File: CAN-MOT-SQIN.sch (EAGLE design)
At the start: 24 parts, among them U1 TLV760, U2 MCP25625ML, U3 BTM7752G, U4 ATTINY816M, Y1 16MHz

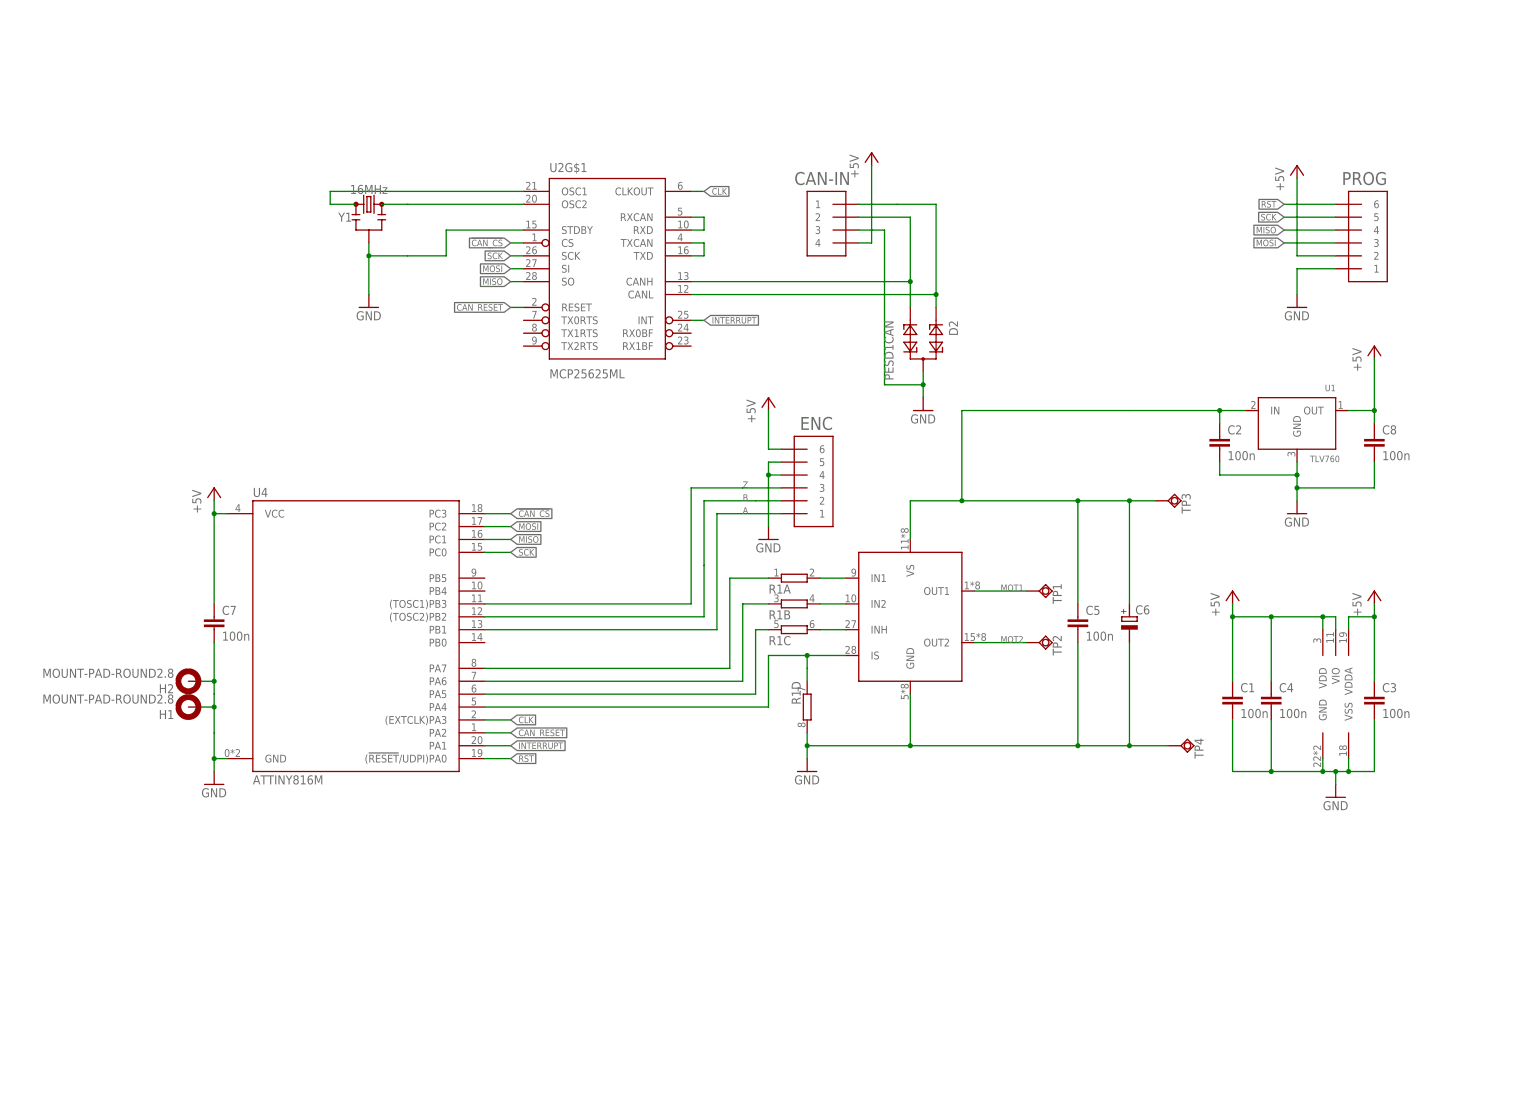
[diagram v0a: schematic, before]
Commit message: Now with better silkscreen
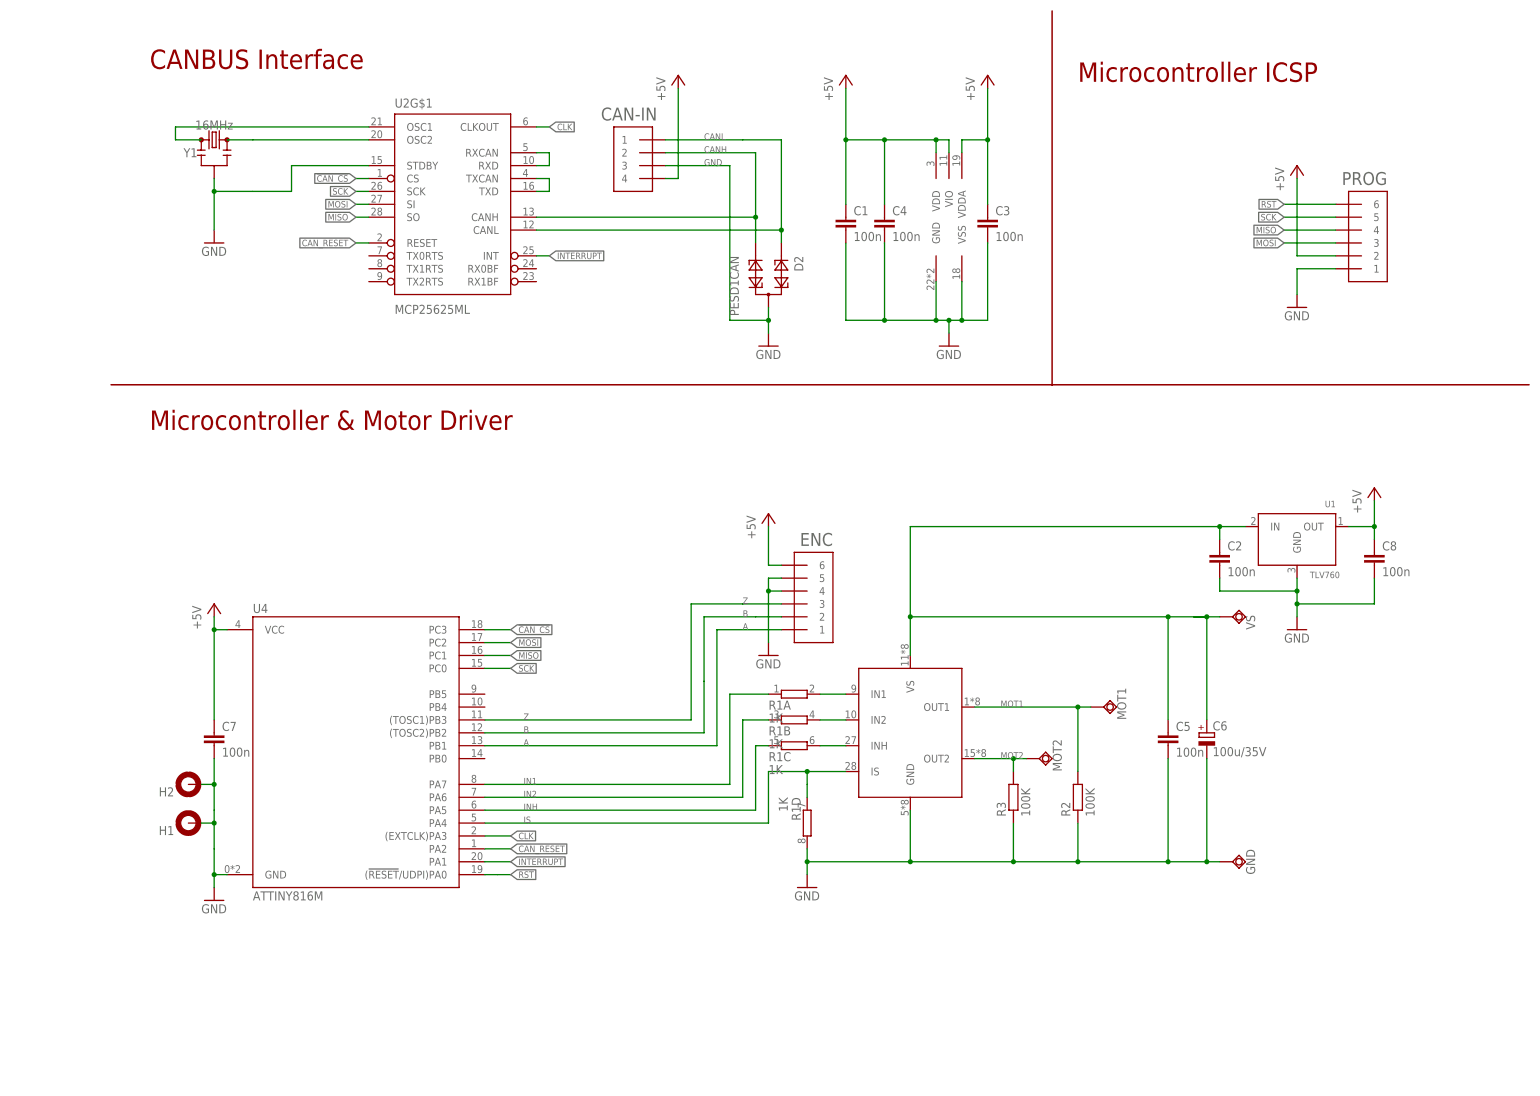
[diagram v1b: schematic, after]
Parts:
- removed TP1, TP2, TP3, TP4: TPSQTP20SQ, testpad:TPSQTP20SQ
- added GND, MOT1, MOT2, VS: TPSQTP20SQ, testpad:TPSQTP20SQ
- added R2, R3: 100K, resistor:R-EU_R0603
- C6: value (none) -> 100u/35V
- R1: value (none) -> 1K
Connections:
- net N$12 renamed IN2
- net N$13 renamed IN1
- net N$4 renamed CANH
- net N$5 renamed CANL
- net N$8 renamed IS
- net N$9 renamed INH
- net GND: now also GND.TP, R2.1, R3.1; no longer TP4.TP
- net MOT1: now also MOT1.TP, R2.2; no longer TP1.TP
- net MOT2: now also MOT2.TP, R3.2; no longer TP2.TP
- net VS: now also VS.TP; no longer TP3.TP
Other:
- note added: "CANBUS Interface"
- note added: "Microcontroller & Motor Driver"
- note added: "Microcontroller ICSP"
- moved on the sheet: C1, C2, C3, C4, C5, C6, C7, C8, CAN-IN, D2, ENC, H1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

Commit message: Re-routed so now the peripherals will do the right thing
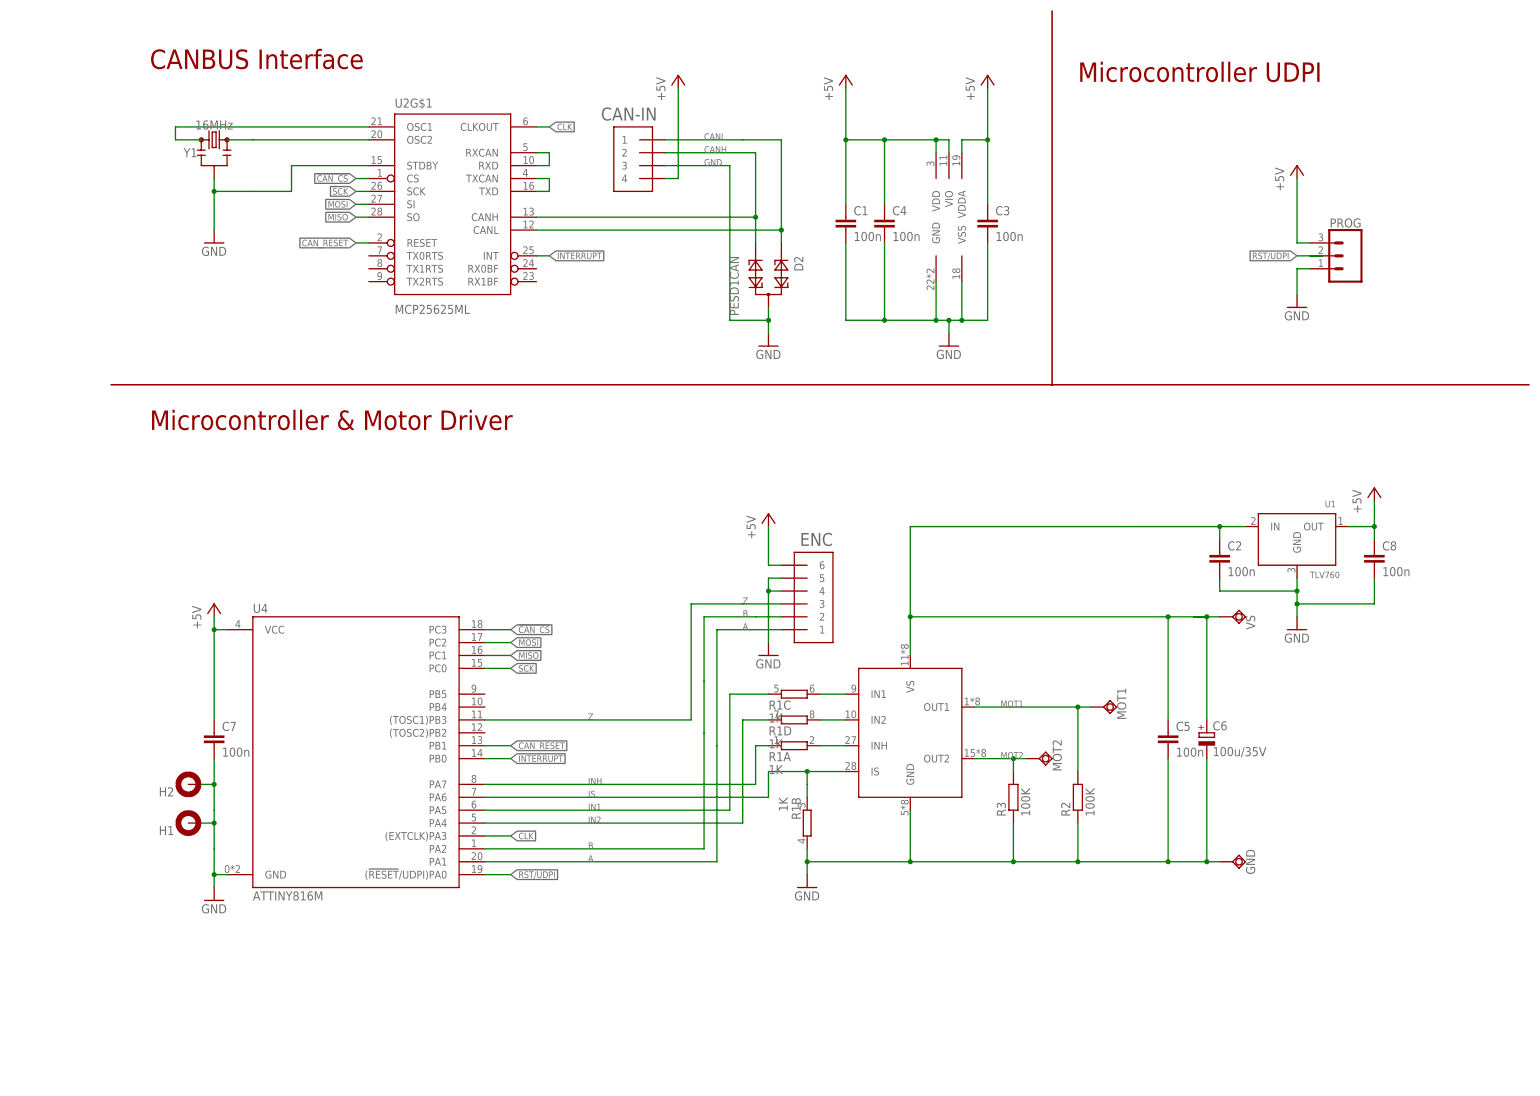
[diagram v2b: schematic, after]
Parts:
- PROG: value STRAWSON_EAGLE_LIB_JST_SH_6 -> (none); device can-library:STRAWSON_EAGLE_LIB_JST_SH_6 -> SparkFun-Connectors:CONN_03LOCK
- Y1: PARTNO (none) -> PRQC16.00CR5010X000
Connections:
- removed net RST: PROG.6, U4.(!RESET!/UDPI)PA0
- new net RST/UDPI: PROG.2, U4.(!RESET!/UDPI)PA0
- net +5V: now also PROG.3; no longer PROG.2
- net A: now also U4.PA1; no longer U4.PB1
- net B: now also U4.PA2; no longer U4.(TOSC2)PB2
- net CAN_RESET: now also U4.PB1; no longer U4.PA2
- net GND: now also R1B.2; no longer R1D.2
- net IN1: now also R1C.1, U4.PA5; no longer R1A.1, U4.PA7
- net IN2: now also R1D.1, U4.PA4; no longer R1B.1, U4.PA6
- net INH: now also R1A.1, U4.PA7; no longer R1C.1, U4.PA5
- net INTERRUPT: now also U4.PB0; no longer U4.PA1
- net IS: now also R1B.1, U4.PA6; no longer R1D.1, U4.PA4
- net MISO: no longer PROG.4
- net MOSI: no longer PROG.3
- net N$3: now also R1C.2; no longer R1A.2
- net N$6: now also R1D.2; no longer R1B.2
- net N$7: now also R1A.2; no longer R1C.2
- net SCK: no longer PROG.5
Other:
- note added: "Microcontroller UDPI"
- note removed: "Microcontroller ICSP"
- moved on the sheet: R1A, R1B, R1C, R1D

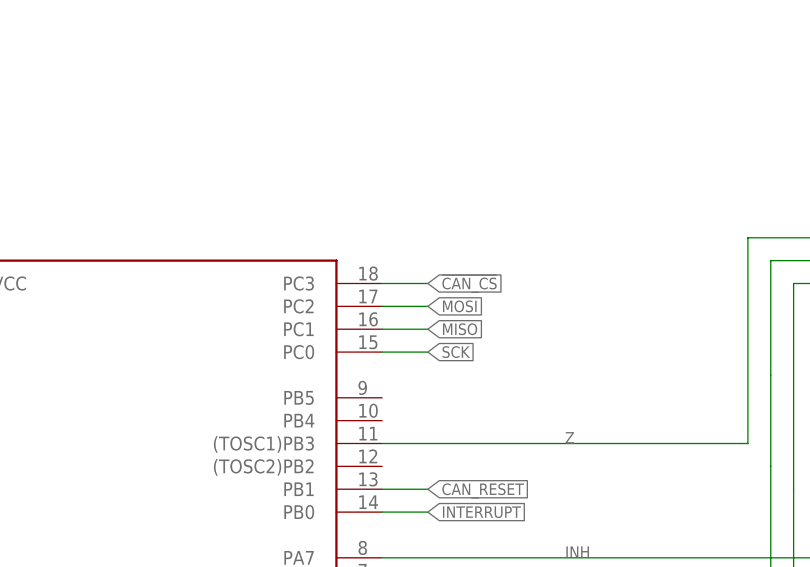
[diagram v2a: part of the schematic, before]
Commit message: Fixed the routing so now it will (probably) work as intended
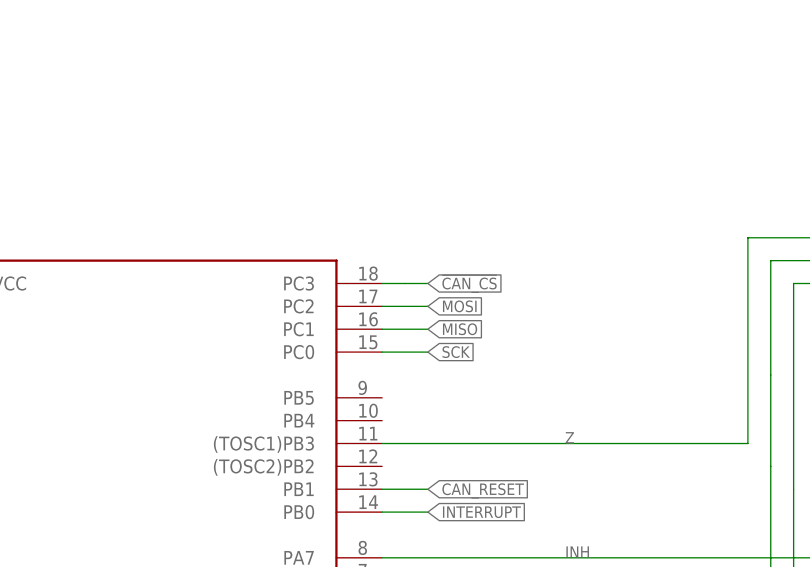
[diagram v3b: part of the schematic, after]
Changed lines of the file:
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@@
 </segment>
 <segment>
-<wire x1="73.66" y1="93.98" x2="78.74" y2="93.98" width="0.1524" layer="91"/>
+<wire x1="73.66" y1="93.98" x2="76.2" y2="93.98" width="0.1524" layer="91"/>
 <label x="78.74" y="93.98" size="1.27" layer="95" xref="yes"/>
 <pinref part="U4" gate="G$1" pin="PC3"/>
+<wire x1="76.2" y1="93.98" x2="78.74" y2="93.98" width="0.1524" layer="91"/>
 </segment>
 </net>
